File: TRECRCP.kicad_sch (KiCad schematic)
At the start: 16 parts, among them SW1 Dispatch2, SW1 Key On/Off Switch, SW2 Maintenince Rotary Switch, SW4 Restart, SW5 Dispatch1, SW8 Stop

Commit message: wip
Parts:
- added 24V_to_5V1: ~, symbol TREC SYMBOL LIB:24v_-{gt}_5v
- added A1: Arduino_Nano_Every, Module:Arduino_Nano, symbol MCU_Module:Arduino_Nano_Every
- added K1: Fujitsu_FTR-LYCA005x, Relay_THT:Relay_SPDT_Fujitsu_FTR-LYCA005x_FormC_Vertical, symbol Relay:Fujitsu_FTR-LYCA005x
- added PS1: HS-40024, Converter_ACDC:Converter_ACDC_Hahn_HS-400xx_THT, symbol Converter_ACDC:HS-40024
- added U1: RoboClaw Motor Controller, symbol custom symbols:RoboClaw_2x30A_MC
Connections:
- new net: 24V_to_5V1.2 (5V), A1.27 (+5V), K1.A2
- new net: A1.29 (GND), A1.4 (GND), PS1.9 (-Vout)
- new net 24V: 24V_to_5V1.1 (24V), K1.11, PS1.7 (+Vout)
- new net NEUT: PS1.1 (AC/N)
- new net VAC: PS1.5 (AC/L)

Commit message: Base elec diagram
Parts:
- added U2, U3: 5304 Gear Motor, symbol custom symbols:5304_Saturn_Gear_Motor
- renumbered 24V_to_5V1 to 24V_to_12V
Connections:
- net at K1.14: now also U1.3 (Vin+)
- net GND: now reaches K1.A1
- net GND: now also 24V_to_12V.3 (GND)
- net at A1.13 (D10): now also U1.S4 (E-STOP)
- net at A1.29 (GND), A1.4 (GND), PS1.9 (-Vout): now also U1.4 (Vin-)
- net at A1.30 (VIN): now also 24V_to_12V.2 (12V)
- net at A1.5 (D2): now also K1.A2
- net at RCC1.10 (UART0_RX): now also U1.S2 (TX)
- net at RCC1.8 (UART0_TX): now also U1.S1 (RX)
- net at U1. (5VDC): now also U2.6 (Ch_B)
- net at U1.1 (M1A): now also U2.1 (M-)
- net at U1.2 (M1B): now also U2.2 (M+)
- net at U1.5 (M2B): now also U3.1 (M-)
- net at U1.6 (M2A): now also U3.2 (M+)
- new net: A1. (USB-B), RCC1. (USB)
- new net: U1. (5VDC), U3.3 (VCC)
- new net: U1. (5VDC), U3.4 (GND)
- new net: U1. (5VDC), U3.5 (Ch_A)
- new net: U1. (5VDC), U3.6 (Ch_B)
- new net: U1. (5VDC), U2.3 (VCC)
- new net: U1. (5VDC), U2.4 (GND)
- new net: U1. (5VDC), U2.5 (Ch_A)
- now unconnected: A1.27 (+5V)
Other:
- note added: "MAKE E-STOP LORE ACCURATE!!"
- note added: "MAKE VCLAMP CIRCUIT HERE :)"
- note added: "NEED TO FIGURE OUT HOW TO HAVE ARDUINO SWITCH RELAY!!"
- moved on the sheet: 24V_to_12V, ESTOP, K1, PS1, SW1, SW2, U1

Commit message: More items!!
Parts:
- added R10, R11, R12, R9: R, symbol Device:R
- added SW3, SW6, SW7, SW9: SW_SPDT_XKB_DMx-xxxx-1, symbol Switch:SW_SPDT_XKB_DMx-xxxx-1
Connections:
- net at ESTOP.1 (A), RCC1.1 (3.3V), SW1.4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: now also SW3.1 (A), SW6.1 (A), SW7.1 (A), SW9.1 (A)
- net at A1.13 (D10), U1.S4 (E-STOP): now also ESTOP.2 (B), R8.2, RCC1.37 (GPIO_26)
- net at A1.2 (RX1): now also RCC1.10 (UART0_RX), U1.S2 (TX)
- net at RCC1.24 (GPIO_8): now also SW7.2 (B)
- net at RCC1.26 (GPIO_7): now also SW9.2 (B)
- net at RCC1.34 (GND): now also R10.1, R11.1, R12.1, R9.1
- net at RCC1.38 (GPIO_20): now also R10.2, SW3.2 (B)
- net at RCC1.40 (GPIO_21): now also R9.2, SW6.2 (B)
- net Drop Down Resistors(10kΩ) renamed Pull Down Resistors(10kΩ)
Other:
- note added: "3.3V"
- note added: "CHECK ELEC CONSTR. W/ SERIAL FOR NANO, PI, & ROBOCLAW"
- note added: "L-BOT"
- note added: "L-TOP"
- note added: "LIMIT SWITCHES"
- note added: "R-BOT"
- note added: "R-TOP"
- company: (none) -> TERRIER RIDE ENGINEERING CLUB
- title: (none) -> RIDE ENGINEERING COMPETITION 2026 ELECTRICAL SCHEMATIC

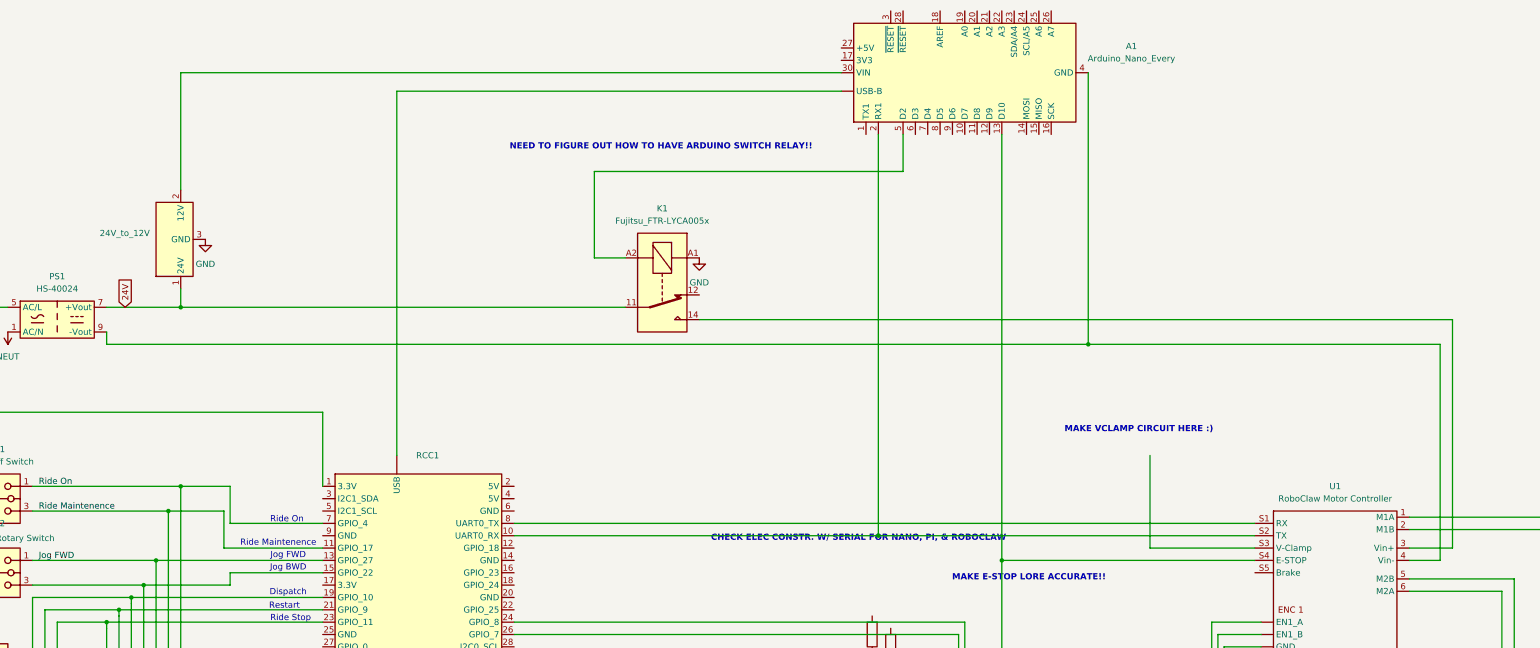
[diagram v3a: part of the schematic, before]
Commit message: Make MOSFET - Relay circuit canon
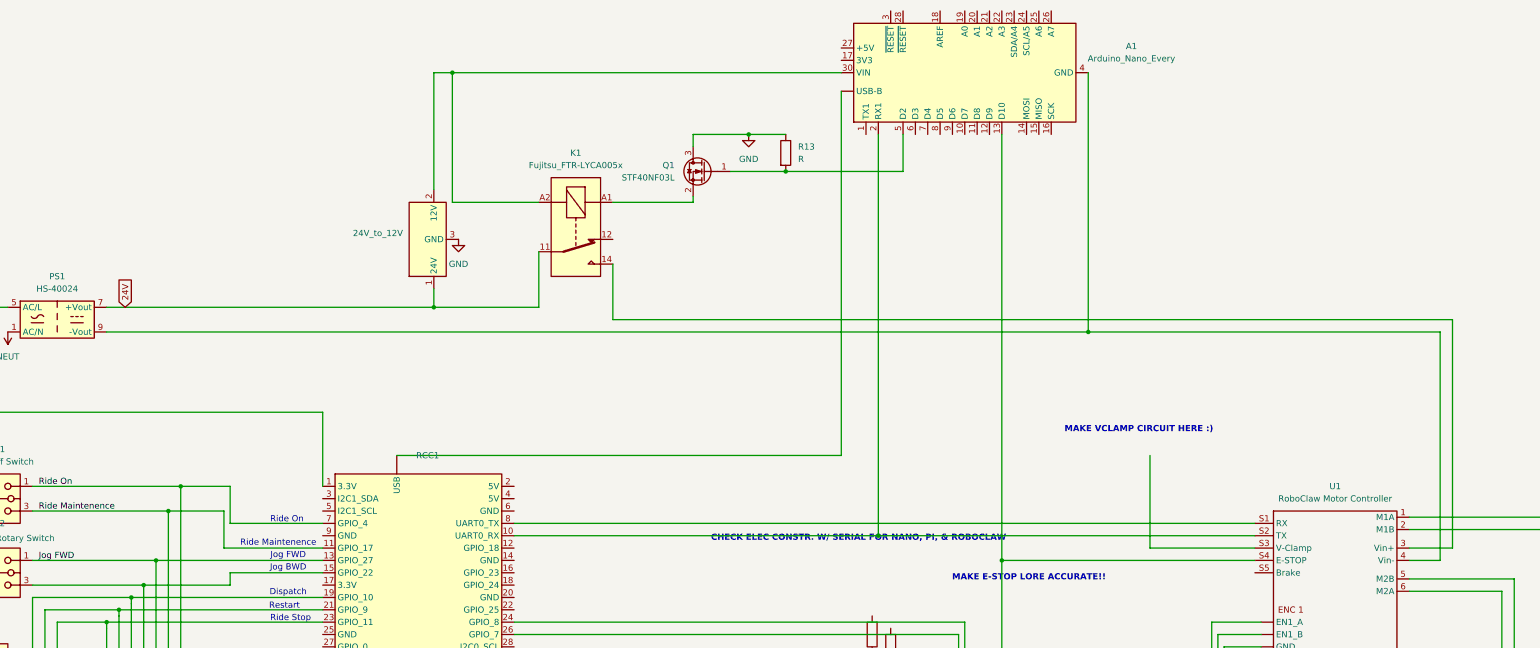
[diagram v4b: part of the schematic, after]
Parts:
- added Q1: STF40NF03L, Package_TO_SOT_SMD:SOT-23, symbol Transistor_FET:2N7002H
- added R13: R, symbol Device:R
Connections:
- net GND: now also Q1.3 (D), R13.1; no longer K1.A1
- net at K1.A2: now also 24V_to_12V.2 (12V), A1.30 (VIN); no longer A1.5 (D2)
- new net: K1.A1, Q1.2 (S)
- new net: A1.5 (D2), Q1.1 (G), R13.2
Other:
- note removed: "NEED TO FIGURE OUT HOW TO HAVE ARDUINO SWITCH RELAY!!"
- moved on the sheet: 24V_to_12V, K1

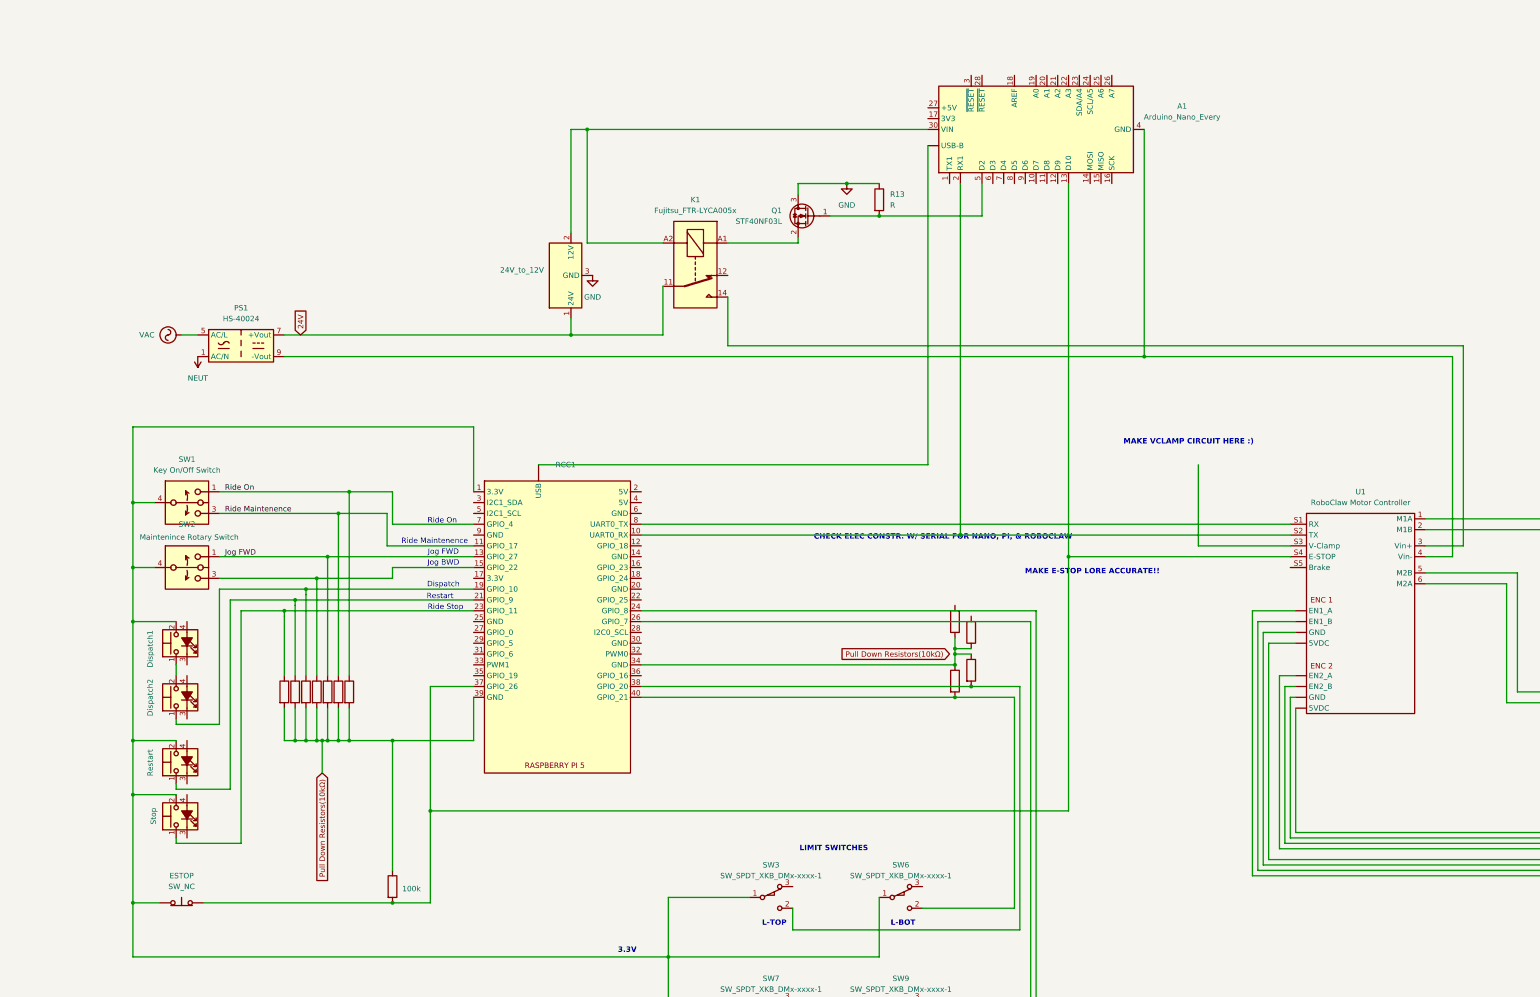
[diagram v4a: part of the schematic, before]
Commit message: Update TRECRCP.kicad_sch
Updated Electrical Schematic(  Fixed communications, added relay circuits for LED, Vclamp Circuit)
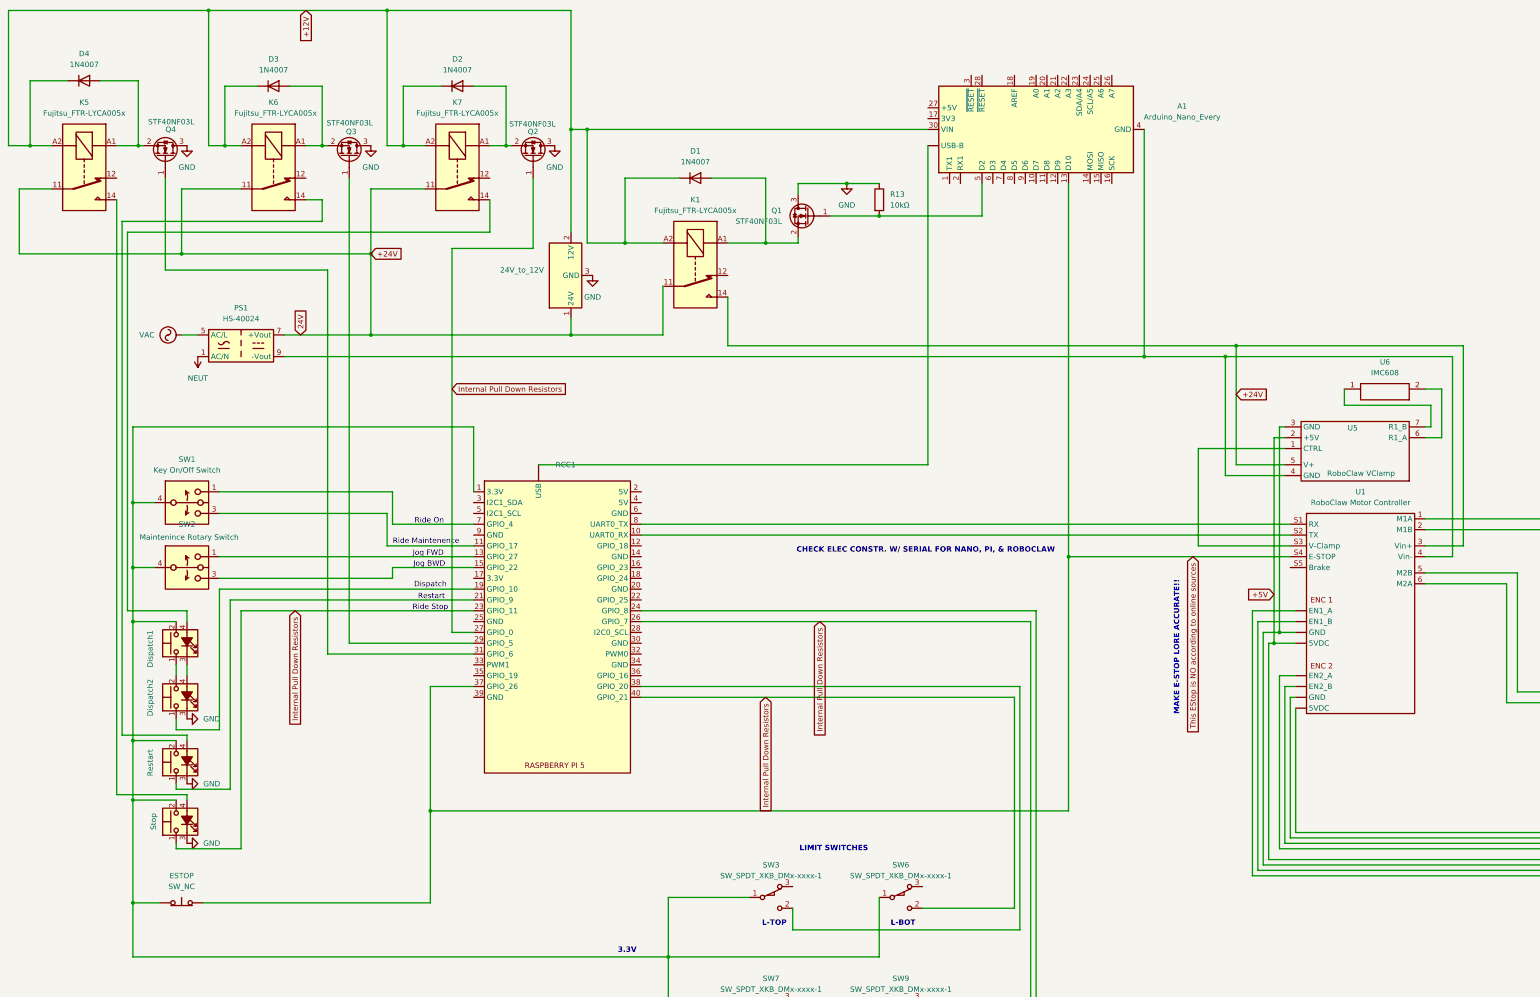
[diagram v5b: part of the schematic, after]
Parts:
- removed R1, R10, R11, R12, R2, R3, R4, R5, R6, R7, R9: R, symbol Device:R
- removed R8: 100k, symbol Device:R
- added D1, D2, D3, D4: 1N4007, Diode_THT:D_DO-41_SOD81_P10.16mm_Horizontal, symbol Diode:1N4007
- added K5, K6, K7: Fujitsu_FTR-LYCA005x, Relay_THT:Relay_SPDT_Fujitsu_FTR-LYCA005x_FormC_Vertical, symbol Relay:Fujitsu_FTR-LYCA005x
- added Q2, Q3, Q4: STF40NF03L, Package_TO_SOT_SMD:SOT-23, symbol Transistor_FET:2N7002H
- added U5: RoboClaw VClamp, symbol CustomSymbols:RoboclawVClamp
- added U6: IMC608, symbol CustomSymbols:Power_Resistor
- R13: value R -> 10kΩ
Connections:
- net 24V is gone; now on net +24V: 24V_to_12V.1 (24V), K1.11, PS1.7 (+Vout)
- net GND: now also SW1.3 (K), SW4.3 (K), SW8.3 (K), Q2.3 (D), Q3.3 (D), Q4.3 (D)
- net Internal Pull Down Resistors: now reaches RCC1.26 (GPIO_7), SW9.2 (B)
- net Internal Pull Down Resistors: now also RCC1.23 (GPIO_11), RCC1.27 (GPIO_0), RCC1.40 (GPIO_21), SW6.2 (B), SW8.1, Q2.1 (G)
- net +24V: now reaches K1.14, U1.3 (Vin+)
- net +24V: now also K5.11, K6.11, K7.11, U5.5 (V+)
- net at K1.A1, Q1.2 (S): now also D1.2 (A)
- net +12V: now reaches 24V_to_12V.2 (12V), A1.30 (VIN), K1.A2
- net +12V: now also D1.1 (K), D2.1 (K), D3.1 (K), D4.1 (K), K5.A2, K6.A2, K7.A2
- net at SW8.4 (A): now also K5.14
- net This EStop is NO according to online sources: now reaches A1.13 (D10), ESTOP.2 (B), RCC1.37 (GPIO_26), U1.S4 (E-STOP)
- net at RCC1.10 (UART0_RX), U1.S2 (TX): no longer A1.2 (RX1)
- net at A1.29 (GND), A1.4 (GND), PS1.9 (-Vout)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: now also U5.4 (GND)
- net at SW5.3 (K): now also SW1.4 (A)
- net at SW5.4 (A): now also K7.14
- net at SW4.4 (A): now also K6.14
- net at RCC1.29 (GPIO_5): now also Q3.1 (G)
- net at RCC1.31 (GPIO_6): now also Q4.1 (G)
- net +5V: now reaches U1. (5VDC), U2.3 (VCC)
- net +5V: now also U5.2 (+5V)
- net at U1. (5VDC), U2.4 (GND): now also U5.3 (GND)
- net at U1.S3 (V-Clamp): now also U5.1 (CTRL)
- net Jog FWD: no longer names the net of RCC1.13 (GPIO_27), SW2.1
- net Pull Down Resistors(10kΩ): no longer names the net of RCC1.39 (GND)
- net Ride Maintenence: no longer names the net of RCC1.11 (GPIO_17), SW1.3
- net Ride On: no longer names the net of RCC1.7 (GPIO_4), SW1.1
- new net: D3.2 (A), K6.A1, Q3.2 (S)
- new net: D2.2 (A), K7.A1, Q2.2 (S)
- new net: D4.2 (A), K5.A1, Q4.2 (S)
- new net: U5.6 (R1_A), U6.2
- new net: U5.7 (R1_B), U6.1
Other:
- note removed: "MAKE VCLAMP CIRCUIT HERE :)"

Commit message: Reformatting & fixes
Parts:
- added D5, D6: LED, symbol Device:LED
- added LL_Mosfet, LL_Mosfet1: P-Channel, Package_TO_SOT_SMD:SOT-23, symbol Transistor_FET:2N7002H
- added R1, R2: R220, symbol Device:R
- added R3: R1k, symbol Device:R
- added SW10: IEC Conn & ON/OFF SW, Button_Switch_SMD:Nidec_Copal_CAS-120A, symbol Switch:SW_Nidec_CAS-120A1
- added U4: ~, symbol TREC SYMBOL LIB:Grounding_Bar
- D1: value 1N4007 -> Flyback Diode
- K1: value Fujitsu_FTR-LYCA005x -> 12v Coil Relay
- SW1: value Key On/Off Switch -> Maint/Off/On Switch
- SW2: value Maintenince Rotary Switch -> Maint Jog Switch
- SW4: value Restart -> Reset
- U6: value IMC608 -> Clamp Resistor
- renumbered Q1 to LL_Mosfet, R13 to Pulldown_Res, U2 to Tower_A, U3 to Tower_B
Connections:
- net +24V: now also D2.1 (K), D3.1 (K), D4.1 (K), K5.A2, K6.A2, K7.A2; no longer 24V_to_12V.1 (24V), K1.11, K5.11, K6.11, K7.11, PS1.7 (+Vout)
- net GND: now also A1.29 (GND), A1.4 (GND), PS1.9 (-Vout), U1.4 (Vin-), U5.4 (GND), D5.1 (K), D6.1 (K), R3.1, U4.1 (GND)
- net VAC: now also SW10.2 (B); no longer PS1.5 (AC/L)
- net Logic High: now reaches ESTOP.1 (A), RCC1.1 (3.3V), SW1.4, SW2.4, SW3.1 (A), SW4.2, SW5.2, SW6.1 (A), SW7.1 (A), SW8.2, SW9.1 (A)
- net at SW8.4 (A): no longer K5.14
- net L Top Limit Switch: now reaches RCC1.38 (GPIO_20), SW3.2 (B)
- net L Top Limit Switch: now also A1.8 (D5)
- net R Top Limit Switch: now reaches RCC1.24 (GPIO_8), SW7.2 (B)
- net R Top Limit Switch: now also A1.10 (D7)
- net Ride On: now reaches RCC1.7 (GPIO_4), SW1.1
- net Ride Maint: now reaches RCC1.11 (GPIO_17), SW1.3
- net Power Enable Signal: now reaches A1.5 (D2), LL_Mosfet.1 (G), Pulldown_Res.2
- net L Bot Limit Switch: now reaches A1.7 (D4)
- net L Bot Limit Switch: now also RCC1.40 (GPIO_21), SW6.2 (B)
- net R Bot Limit Switch: now reaches A1.9 (D6)
- net R Bot Limit Switch: now also RCC1.26 (GPIO_7), SW9.2 (B)
- net at SW5.4 (A): no longer K7.14
- net Reset LED Control: now reaches Q3.1 (G), RCC1.29 (GPIO_5)
- net Dispatch: now reaches RCC1.19 (GPIO_10), SW1.1
- net Reset: now reaches RCC1.21 (GPIO_9), SW4.1
- net at SW4.4 (A): no longer K6.14
- net Jog Up: now reaches RCC1.13 (GPIO_27), SW2.1
- net Jog Down: now reaches RCC1.15 (GPIO_22), SW2.3
- net Dispatch LED Control: now reaches RCC1.31 (GPIO_6)
- net Dispatch LED Control: now also Q2.1 (G); no longer Q4.1 (G)
- net RCC E-Stop Trigger: now reaches RCC1.36 (GPIO_16)
- net RCC E-Stop Trigger: now also LL_Mosfet1.1 (G)
- removed net +12V: 24V_to_12V.2 (12V), A1.30 (VIN), D1.1 (K), D2.1 (K), D3.1 (K), D4.1 (K), K1.A2, K5.A2, K6.A2, K7.A2
- removed net Internal Pull Down Resistors: Q2.1 (G), RCC1.23 (GPIO_11), RCC1.26 (GPIO_7), RCC1.27 (GPIO_0), RCC1.40 (GPIO_21), SW6.2 (B), SW8.1, SW9.2 (B)
- removed net This EStop is NO according to online sources: A1.13 (D10), ESTOP.2 (B), RCC1.37 (GPIO_26), U1.S4 (E-STOP)
- new net: LL_Mosfet.3 (D), LL_Mosfet1.2 (S), R1.2
- new net: D5.2 (A), R1.1
- new net: D6.2 (A), R2.1
- new net 120VAC: K5.11, K6.11, K7.11, PS1.5 (AC/L), SW10.1 (C)
- new net 12VDC: 24V_to_12V.2 (12V), A1.30 (VIN), D1.1 (K), K1.A2
- new net 24V: 24V_to_12V.1 (24V), K1.11, PS1.7 (+Vout)
- new net Dispatch LED Power (120VAC): K5.14
- new net E-Stop Button: ESTOP.2 (B), LL_Mosfet.2 (S), R2.2
- new net E-Stop Signal Out: LL_Mosfet1.3 (D), R3.2, U1.S4 (E-STOP)
- new net PLC E-Stop Trigger: A1.13 (D10), LL_Mosfet.1 (G)
- new net Stop: RCC1.23 (GPIO_11), SW8.1
- new net Stop LED Control: Q4.1 (G), RCC1.27 (GPIO_0)
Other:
- note added: "E-STOP CIRCUIT"
- note added: "If ANY of the inputs go to their "off" state, the E-Stop will be On."
- note added: "POWER ENABLE CIRCUIT"
- note added: "PUSHBUTTON LED DRIVER"
- note removed: "3.3V"
- note removed: "CHECK ELEC CONSTR. W/ SERIAL FOR NANO, PI, & ROBOCLAW"
- note removed: "Dispatch"
- note removed: "Jog BWD"
- note removed: "Jog FWD"
- note removed: "MAKE E-STOP LORE ACCURATE!!"
- note removed: "Restart"
- note removed: "Ride Maintenence"
- note removed: "Ride On"
- note removed: "Ride Stop"
- moved on the sheet: 24V_to_12V, A1, D2, D3, D4, ESTOP, K5, K6, K7, LL_Mosfet, PS1, Pulldown_Res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

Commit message: some more improvements
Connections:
- net Ride On is gone; now on net On Key Switch: RCC1.7 (GPIO_4), SW1.1
- net Dispatch LED Control: now also RCC1.27 (GPIO_0); no longer RCC1.31 (GPIO_6)
- net Dispatch LED Power (120VAC): now also K7.14, SW5.4 (A); no longer K5.14
- net Reset LED Power (120VAC): now also K6.14, SW4.4 (A)
- net Stop LED Control: now also RCC1.31 (GPIO_6); no longer RCC1.27 (GPIO_0)
- net Stop LED Power (120VAC): now also K5.14, SW8.4 (A)
- net On Key Switch: now reaches A1.6 (D3)

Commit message: update
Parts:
- added D7: Flyback Diode, Diode_THT:D_DO-41_SOD81_P10.16mm_Horizontal, symbol Diode:1N4007
- added K2: 12v Coil Relay, Relay_THT:Relay_SPDT_Fujitsu_FTR-LYCA005x_FormC_Vertical, symbol Relay:Fujitsu_FTR-LYCA005x
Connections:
- net 24V is gone; now on net +24V: 24V_to_12V.1 (24V), K1.11, PS1.7 (+Vout)
- net 12VDC: now also D7.1 (K), K2.A2
- net at D1.2 (A), K1.A1, LL_Mosfet.2 (S): now also D7.2 (A), K2.A1
- net 120VAC renamed 120V
- net 120V: now also K2.11, K2.14
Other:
- moved on the sheet: 24V_to_12V, A1, LL_Mosfet, PS1, Pulldown_Res
